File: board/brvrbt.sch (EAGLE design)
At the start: 9 parts

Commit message: layout
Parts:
- R1, R2: device adafruit:R-US_0207/12 -> adafruit:R-US_0207/7
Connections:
- net AGND renamed GND
- net N$1 renamed BASE_2
- net N$2 renamed COLLECTOR_2
- net N$3 renamed BASE_1
- net N$4 renamed COLLECTOR_1
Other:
- moved on the sheet: BATTERY, EYE1, EYE2, LEG1, LEG2, NPN_1, NPN_2

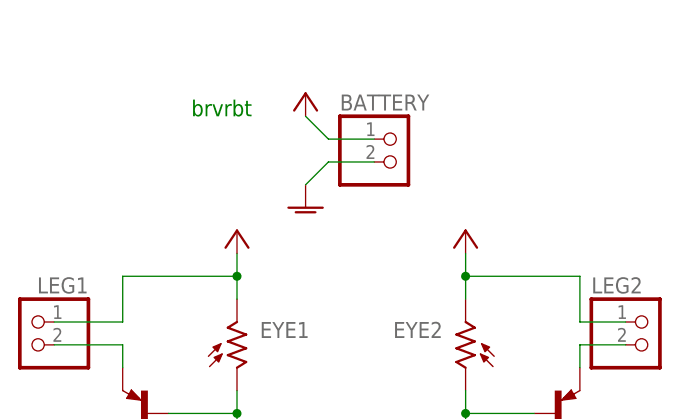
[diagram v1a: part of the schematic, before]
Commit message: small footprint 23x19mm
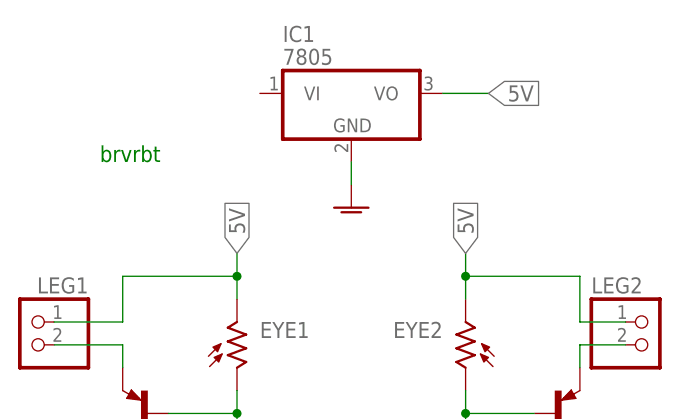
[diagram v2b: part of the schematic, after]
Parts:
- removed BATTERY: (no value), microbuilder:HEADER-1X2
- added IC1: 7805, linear:7805TV
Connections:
- removed net VCC: BATTERY.1, EYE1.2, EYE2.2, LEG1.1, LEG2.1
- new net 5V: EYE1.2, EYE2.2, IC1.VO, LEG1.1, LEG2.1
- net GND: now also IC1.GND; no longer BATTERY.2

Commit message: silk work
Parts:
- NPN_2: value (none) -> E B C
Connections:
- new net IN_BATT: IC1.VI
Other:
- note added: "B"
- note added: "C"
- note added: "E"
- note added: "b"
- note added: "c"
- note added: "e"
- moved on the sheet: EYE1, EYE2, IC1, LEG1, LEG2, NPN_1, NPN_2
